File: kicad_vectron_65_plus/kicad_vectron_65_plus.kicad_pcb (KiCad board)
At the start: 4 copper layers, 131.1 x 79.4 mm, 48 parts, among them J1 Power, J2 Power, J3 VIA 1 Ports, J4 Conn_01x16_Male, J5 PS/2 Keyboard, J6 Power, J7 Power, U1 W65C02SxP, U10 SN74LS08N, U11 SN74HC32N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

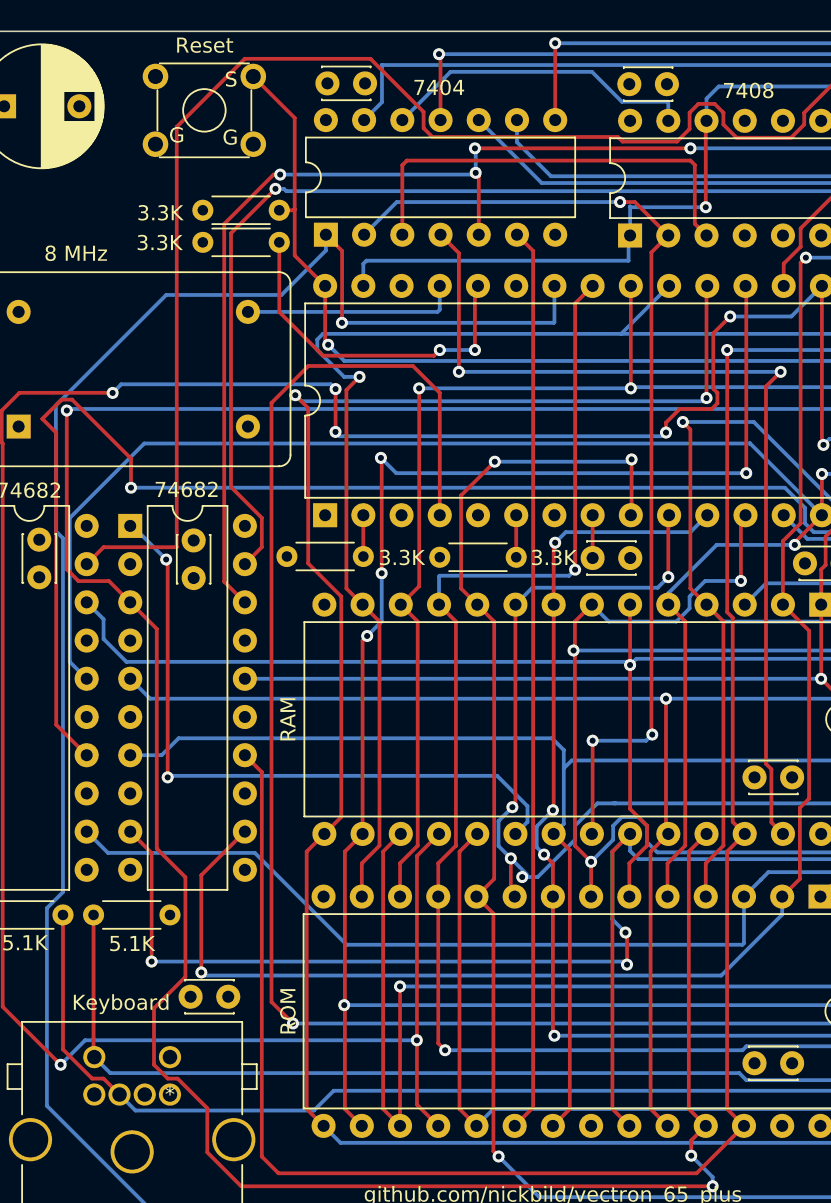
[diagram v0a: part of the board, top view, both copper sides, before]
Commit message: Mirror image for PS/2 connection.
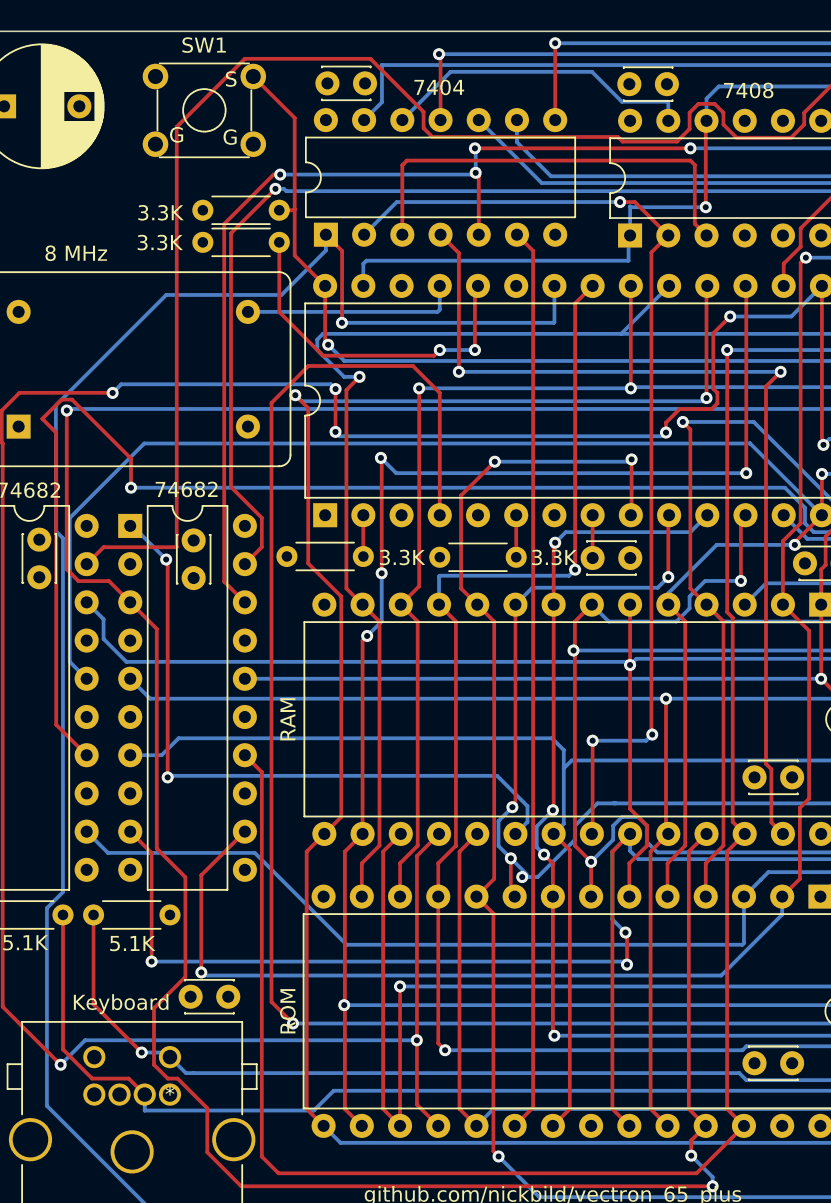
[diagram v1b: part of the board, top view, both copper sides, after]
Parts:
- renumbered Reset to SW1
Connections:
- J5 pad 1: Net-(J4-Pad14) -> Net-(J5-Pad1)
- J5 pad 2: Net-(J5-Pad2) -> Net-(J4-Pad14)
- J5 pad 3: GND -> +5V
- J5 pad 4: +5V -> GND
- J5 pad 5: Net-(J4-Pad13) -> Net-(J5-Pad5)
- J5 pad 6: Net-(J5-Pad6) -> Net-(J4-Pad13)
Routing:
- net Net-(J4-Pad13): track 102.1 -> 100.1 mm, vias 0 -> 1
- net Net-(J4-Pad14): track 107.2 -> 107.9 mm
